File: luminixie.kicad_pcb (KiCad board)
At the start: 2 copper layers, 27 parts, among them J1 Conn_01x03_Female, U1 ESP32-MINIKIT, U2 HV-POWER, U3 HV5530_PLCC, U4 HV5530_PLCC

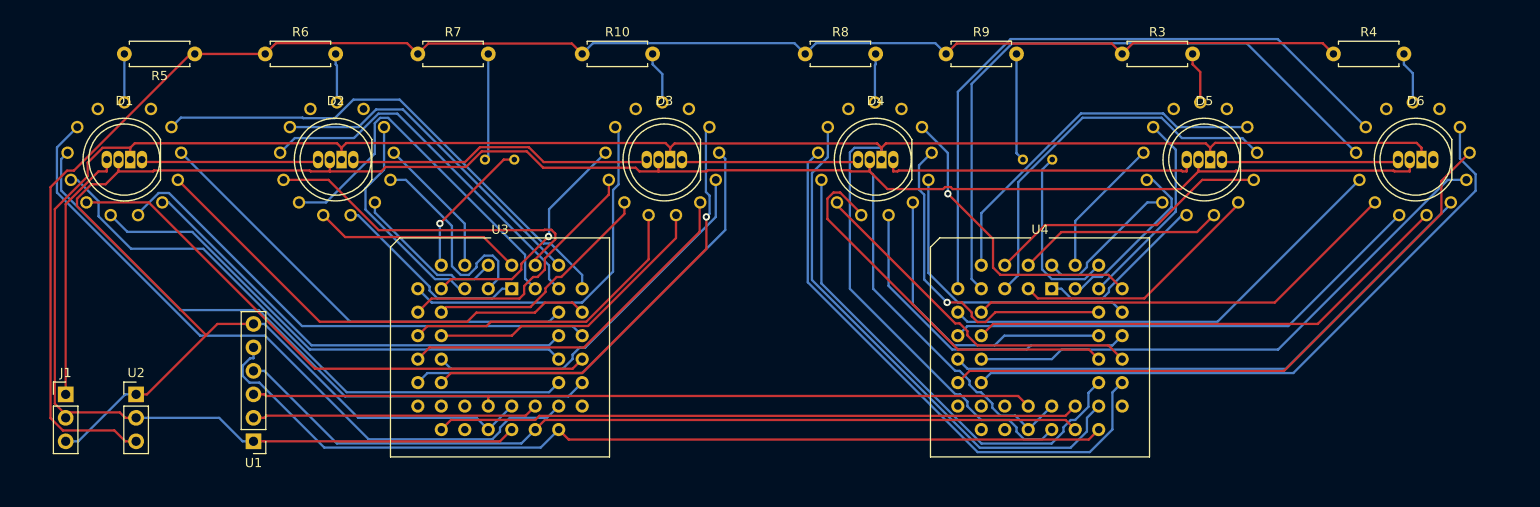
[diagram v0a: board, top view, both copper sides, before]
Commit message: Add drillholes, add Luminixie logo, add edge cuts, delete netlist, add dependencies (apa-106, nixies)
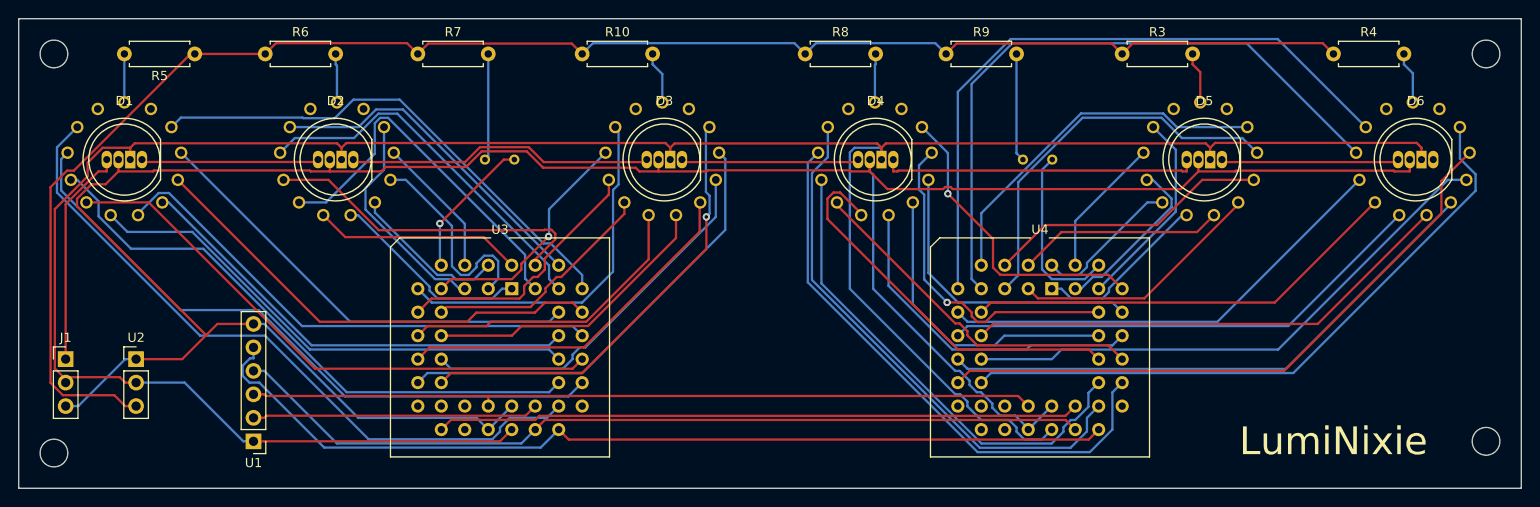
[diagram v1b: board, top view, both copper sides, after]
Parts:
- added REF**: MountingHole_3mm, MountingHole:MountingHole_3mm, F.Cu at (83.8, 105.4)
- added REF**: MountingHole_3mm, MountingHole:MountingHole_3mm, F.Cu at (83.8, 62.2)
- added REF**: MountingHole_3mm, MountingHole:MountingHole_3mm, F.Cu at (238.8, 62.2)
- added REF**: MountingHole_3mm, MountingHole:MountingHole_3mm, F.Cu at (238.8, 104.1)
- moved J1 3.81 mm to (85.1, 95.2)
- moved U2 3.81 mm to (92.7, 95.2)
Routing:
- net Net-(R10-Pad1): track 185.8 -> 182.0 mm
- net DIN: track 27.8 -> 24.0 mm
- net GND: track 283.7 -> 281.5 mm
- net +5V: track 278.1 -> 276.5 mm
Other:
- board outline added: 162.6 x 50.8 mm
- board text added: "LumiNixie"
